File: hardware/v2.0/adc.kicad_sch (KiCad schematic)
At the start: 26 parts, among them IC2 LTC2256CUJ-12#PBF, J7 RSP-122811-01, U1 ECP5U-25F-CABGA256, U11 LT1993CUD-2_PBF, U13 TCR5FM50A, Y2 SG-8018CG 25.000000MHz

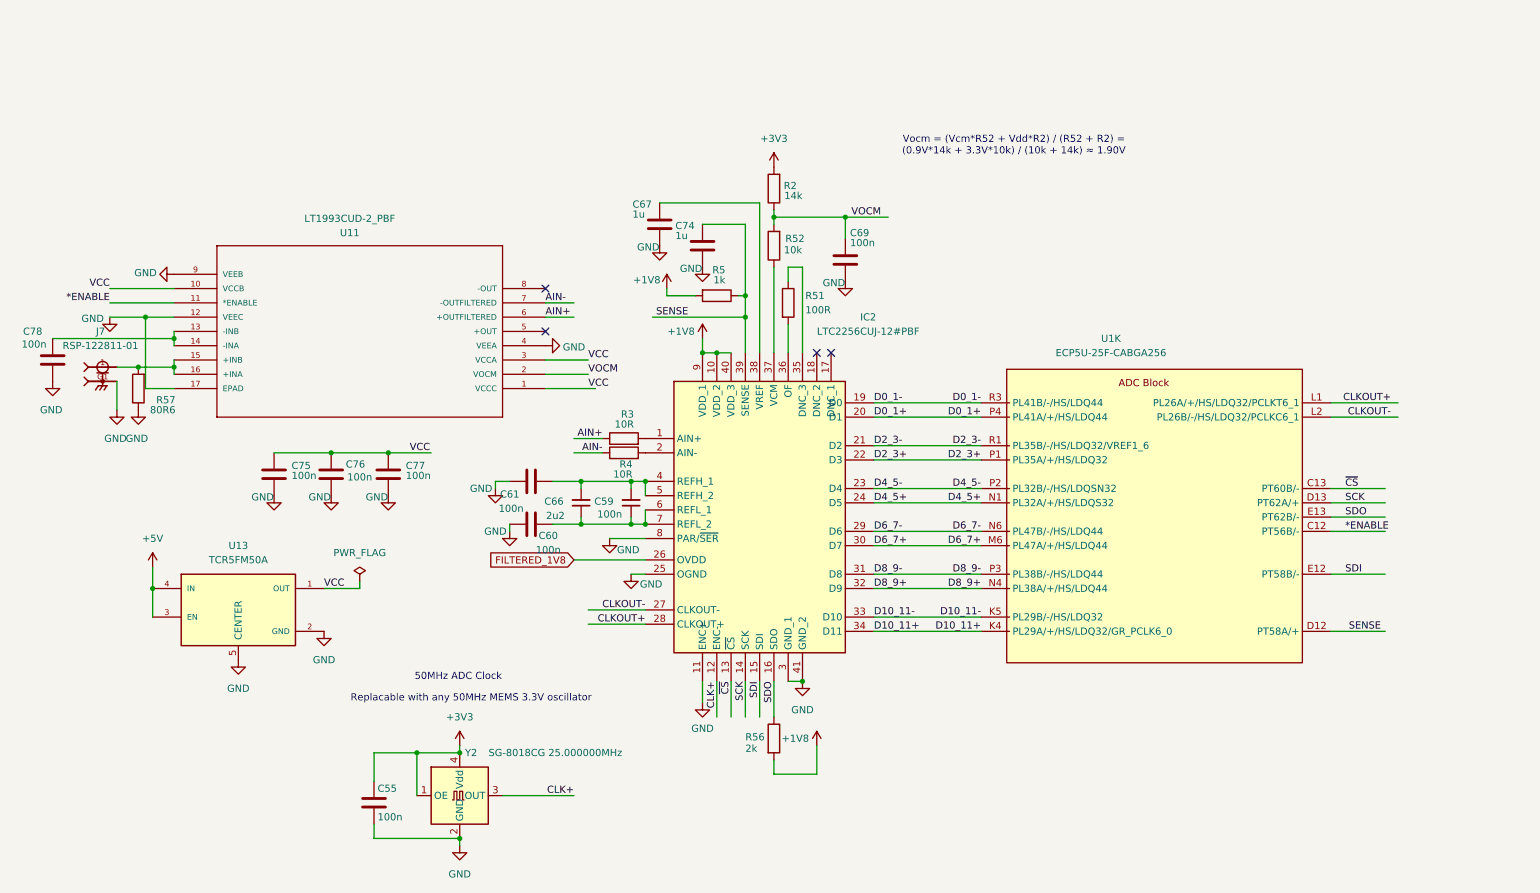
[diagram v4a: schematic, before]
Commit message: Grouped FPGA, ADC, ADC Driver, LEDs IC
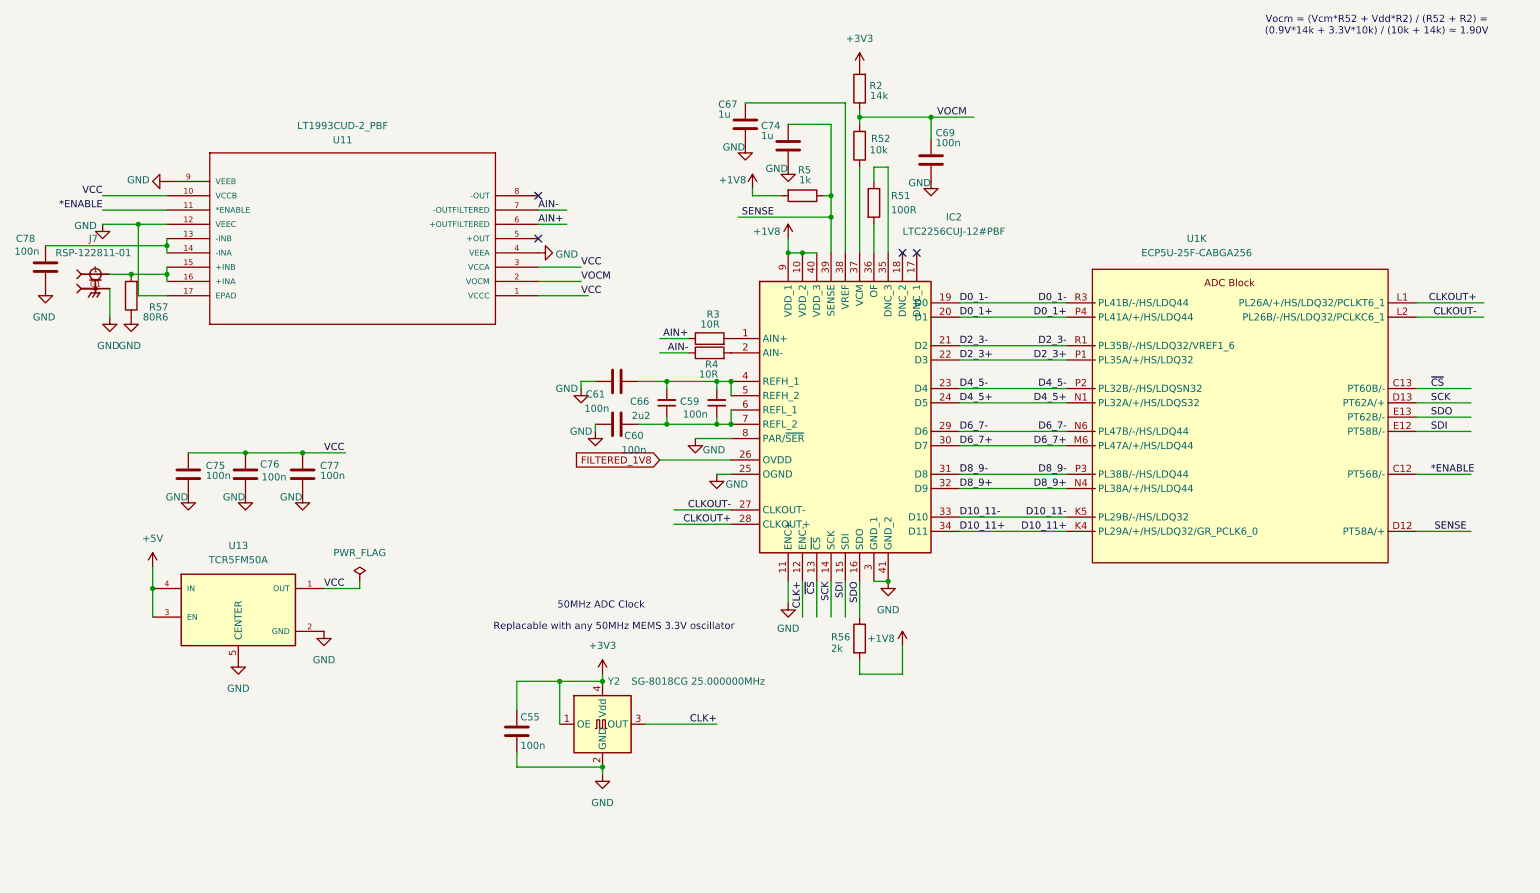
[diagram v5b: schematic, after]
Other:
- moved on the sheet: C55, C59, C60, C61, C66, C67, C69, C74, C75, C76, C77, C78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

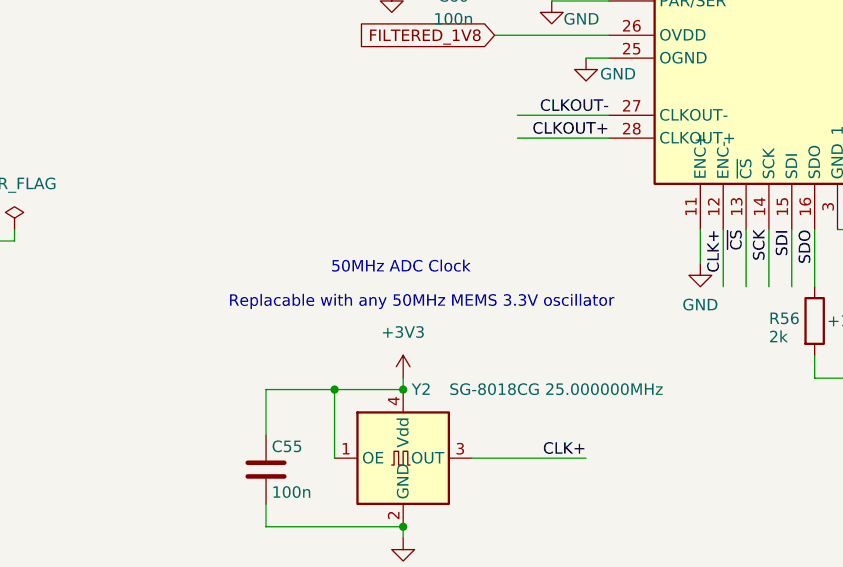
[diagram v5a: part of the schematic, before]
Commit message: Clock label fix
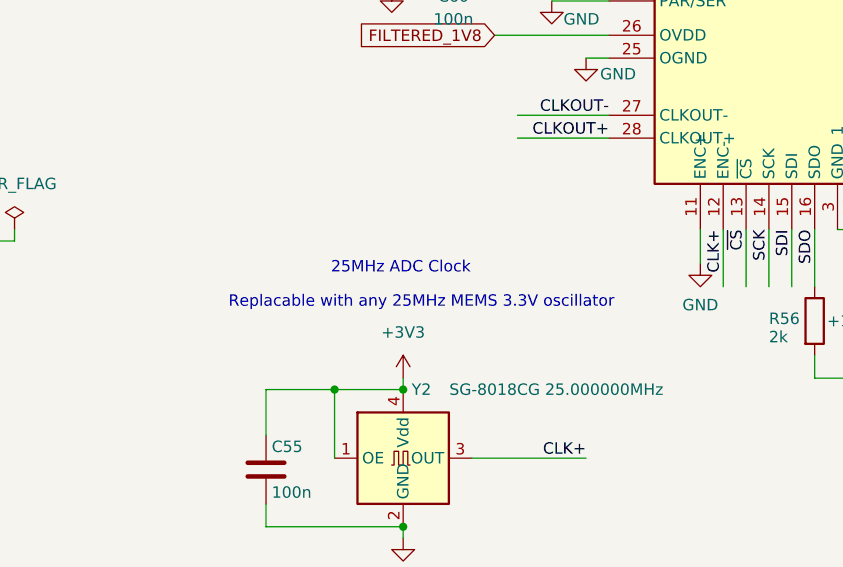
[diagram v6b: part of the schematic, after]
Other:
- note added: "25MHz ADC Clock"
- note added: "Replacable with any 25MHz MEMS 3.3V oscillator"
- note removed: "50MHz ADC Clock"
- note removed: "Replacable with any 50MHz MEMS 3.3V oscillator"
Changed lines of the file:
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@@
 		)
 	)
-	(text "50MHz ADC Clock"
+	(text "25MHz ADC Clock"
 		(exclude_from_sim no)
 		(at 119.126 122.428 0)
@@
 		)
 	)
-	(text "Replacable with any 50MHz MEMS 3.3V oscillator"
+	(text "Replacable with any 25MHz MEMS 3.3V oscillator"
 		(exclude_from_sim no)
 		(at 121.412 126.238 0)

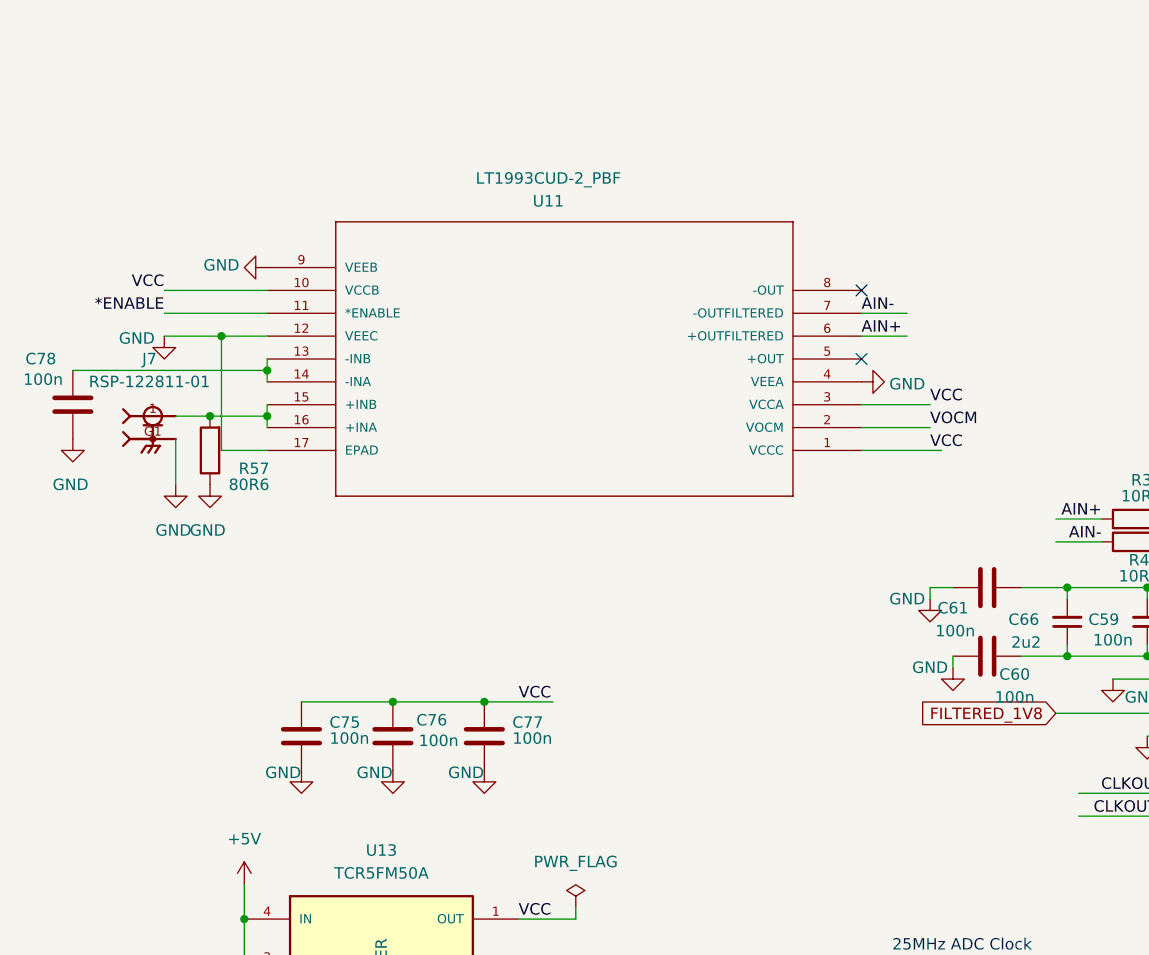
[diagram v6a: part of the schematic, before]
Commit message: ADC driver power pins bypass
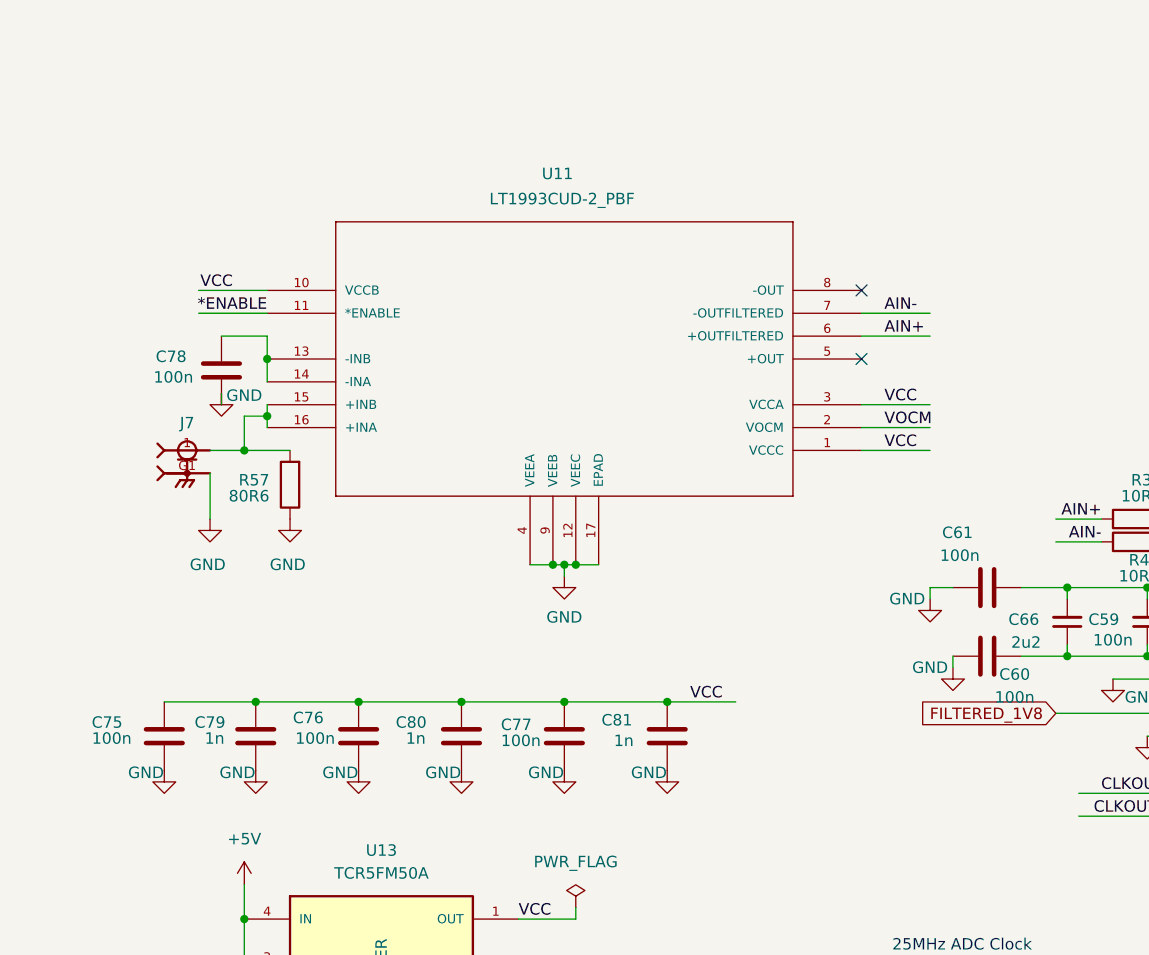
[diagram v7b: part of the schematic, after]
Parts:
- added C79, C80, C81: 1n, Capacitor_SMD:C_0402_1005Metric, symbol Device:C
- U11: MANUFACTURER_PART_NUMBER LT1993CUD-2#PBF -> lt1993cud2
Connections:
- net GND: now also C79.2, C80.2, C81.2
- net VCC: now also C79.1, C80.1, C81.1
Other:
- moved on the sheet: C75, C76, C77, C78, J7, R57, U11

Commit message: Repo links update
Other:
- title: Icepi Zero -> GammaPi Zero
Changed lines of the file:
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@@
 	(paper "A4")
 	(title_block
-		(title "Icepi Zero")
-		(date "2026-01-17")
-		(rev "v2.1")
+		(title "GammaPi Zero")
+		(date "2026-01-25")
+		(rev "v2.3.2")
 		(company "Vadym Vikulin, Chengyin Yao (cheyao)")
-		(comment 1 "https://github.com/vikulin/icepi-zero")
+		(comment 1 "https://github.com/vikulin/gammapi-zero")
 		(comment 2 "License: Solderpad")
 		(comment 9 "OSHWA FR000026")
